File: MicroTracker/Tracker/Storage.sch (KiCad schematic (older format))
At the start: 5 parts, among them J4 Micro_SD_Card

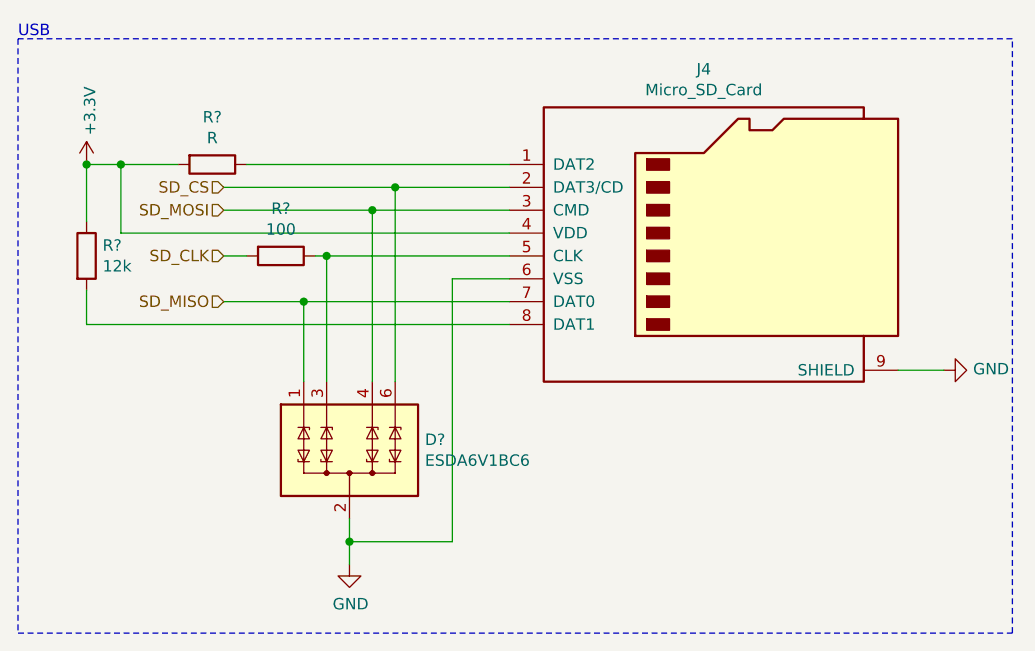
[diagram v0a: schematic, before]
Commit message: added charges
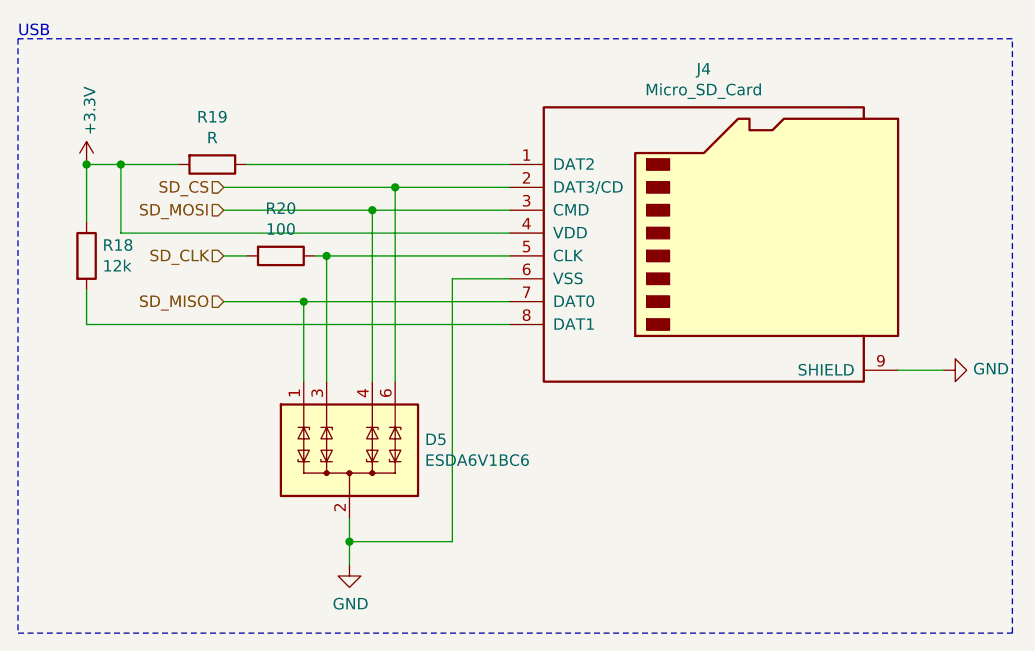
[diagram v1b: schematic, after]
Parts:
- gave numbers to parts that had none: 4
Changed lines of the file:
@@
 SD_MOSI
 $Comp
-L Device:R R?
+L Device:R R19
 U 1 1 5F055498
 P 4050 3050
-F 0 "R?" V 3843 3050 50  0000 C CNN
+F 0 "R19" V 3843 3050 50  0000 C CNN
 F 1 "R" V 3934 3050 50  0000 C CNN
 F 2 "" V 3980 3050 50  0001 C CNN
@@
 	4100 3250 4750 3250
 $Comp
-L Device:R R?
+L Device:R R18
 U 1 1 5F05B559
 P 3500 3450
-F 0 "R?" H 3570 3496 50  0000 L CNN
+F 0 "R18" H 3570 3496 50  0000 L CNN
 F 1 "12k" H 3570 3405 50  0000 L CNN
 F 2 "" V 3430 3450 50  0001 C CNN
@@
 	4100 3650 4450 3650
 $Comp
-L Device:R R?
+L Device:R R20
 U 1 1 5F05CDAB
 P 4350 3450
-F 0 "R?" V 4143 3450 50  0000 C CNN
+F 0 "R20" V 4143 3450 50  0000 C CNN
 F 1 "100" V 4234 3450 50  0000 C CNN
 F 2 "" V 4280 3450 50  0001 C CNN
@@
 	4500 3450 4550 3450
 $Comp
-L Power_Protection:ESDA6V1BC6 D?
+L Power_Protection:ESDA6V1BC6 D5
 U 1 1 5F05DAB7
 P 4650 4300
-F 0 "D?" H 4980 4346 50  0000 L CNN
+F 0 "D5" H 4980 4346 50  0000 L CNN
 F 1 "ESDA6V1BC6" H 4980 4255 50  0000 L CNN
 F 2 "Package_TO_SOT_SMD:SOT-23-6" H 4650 3950 50  0001 C CNN
@@
 $EndComp
 $Comp
-L power:GND #PWR?
+L power:GND #PWR0156
 U 1 1 5F06B02C
 P 4650 4800
-F 0 "#PWR?" H 4650 4550 50  0001 C CNN
+F 0 "#PWR0156" H 4650 4550 50  0001 C CNN
 F 1 "GND" H 4655 4627 50  0000 C CNN
 F 2 "" H 4650 4800 50  0001 C CNN

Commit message: assigned parts
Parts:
- J4: footprint (none) -> Connector_Card:microSD_HC_Hirose_DM3BT-DSF-PEJS
- R18, R19, R20: footprint (none) -> Resistor_SMD:R_0805_2012Metric_Pad1.15x1.40mm_HandSolder
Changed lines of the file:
@@
 F 0 "J4" H 6200 4067 50  0000 C CNN
 F 1 "Micro_SD_Card" H 6200 3976 50  0000 C CNN
-F 2 "" H 7400 3650 50  0001 C CNN
+F 2 "Connector_Card:microSD_HC_Hirose_DM3BT-DSF-PEJS" H 7400 3650 50  0001 C CNN
 F 3 "http://katalog.we-online.de/em/datasheet/693072010801.pdf" H 6250 3350 50  0001 C CNN
 	1    6250 3350
@@
 F 0 "R19" V 3843 3050 50  0000 C CNN
 F 1 "R" V 3934 3050 50  0000 C CNN
-F 2 "" V 3980 3050 50  0001 C CNN
+F 2 "Resistor_SMD:R_0805_2012Metric_Pad1.15x1.40mm_HandSolder" V 3980 3050 50  0001 C CNN
 F 3 "~" H 4050 3050 50  0001 C CNN
 	1    4050 3050
@@
 F 0 "R18" H 3570 3496 50  0000 L CNN
 F 1 "12k" H 3570 3405 50  0000 L CNN
-F 2 "" V 3430 3450 50  0001 C CNN
+F 2 "Resistor_SMD:R_0805_2012Metric_Pad1.15x1.40mm_HandSolder" V 3430 3450 50  0001 C CNN
 F 3 "~" H 3500 3450 50  0001 C CNN
 	1    3500 3450
@@
 F 0 "R20" V 4143 3450 50  0000 C CNN
 F 1 "100" V 4234 3450 50  0000 C CNN
-F 2 "" V 4280 3450 50  0001 C CNN
+F 2 "Resistor_SMD:R_0805_2012Metric_Pad1.15x1.40mm_HandSolder" V 4280 3450 50  0001 C CNN
 F 3 "~" H 4350 3450 50  0001 C CNN
 	1    4350 3450
